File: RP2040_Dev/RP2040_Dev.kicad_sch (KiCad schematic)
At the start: 40 parts, among them J1 USB4105-GF-A, J2 Conn_01x18_Pin, J3 Conn_01x18_Pin, SW1 SW_Push, SW2 SW_Push, U1 RP2040, U2 W25Q128JVS, U4 AMS1117CS-3.3, Y1 ABM8G-12.000MHZ-4Y-T3

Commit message: rp2040 update
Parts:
- C1, C10, C11, C12, C13, C14, C15, C16, C17, C2, C3, C4, C5, C6, C7, C8, C9: footprint Capacitor_SMD:C_0402_1005Metric_Pad0.74x0.62mm_HandSolder -> Capacitor_SMD:C_0201_0603Metric_Pad0.64x0.40mm_HandSolder
- R1, R10, R2, R3, R4, R5, R6, R7, R8, R9: footprint Resistor_SMD:R_0402_1005Metric_Pad0.72x0.64mm_HandSolder -> Resistor_SMD:R_0201_0603Metric_Pad0.64x0.40mm_HandSolder
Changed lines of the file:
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@@
 			)
 		)
-		(property "Footprint" "Capacitor_SMD:C_0402_1005Metric_Pad0.74x0.62mm_HandSolder"
+		(property "Footprint" "Capacitor_SMD:C_0201_0603Metric_Pad0.64x0.40mm_HandSolder"
 			(at 146.05 63.5 0)
 			(effects
@@
 			)
 		)
-		(property "Footprint" "Capacitor_SMD:C_0402_1005Metric_Pad0.74x0.62mm_HandSolder"
+		(property "Footprint" "Capacitor_SMD:C_0201_0603Metric_Pad0.64x0.40mm_HandSolder"
 			(at 59.3852 121.92 0)
 			(effects
@@
 			)
 		)
-		(property "Footprint" "Capacitor_SMD:C_0402_1005Metric_Pad0.74x0.62mm_HandSolder"
+		(property "Footprint" "Capacitor_SMD:C_0201_0603Metric_Pad0.64x0.40mm_HandSolder"
 			(at 115.2652 160.02 0)
 			(effects
@@
 			)
 		)
-		(property "Footprint" "Capacitor_SMD:C_0402_1005Metric_Pad0.74x0.62mm_HandSolder"
+		(property "Footprint" "Capacitor_SMD:C_0201_0603Metric_Pad0.64x0.40mm_HandSolder"
 			(at 115.2652 40.64 0)
 			(effects
@@
 			)
 		)
-		(property "Footprint" "Capacitor_SMD:C_0402_1005Metric_Pad0.74x0.62mm_HandSolder"
+		(property "Footprint" "Capacitor_SMD:C_0201_0603Metric_Pad0.64x0.40mm_HandSolder"
 			(at 270.51 33.02 0)
 			(effects
@@
 			)
 		)
-		(property "Footprint" "Resistor_SMD:R_0402_1005Metric_Pad0.72x0.64mm_HandSolder"
+		(property "Footprint" "Resistor_SMD:R_0201_0603Metric_Pad0.64x0.40mm_HandSolder"
 			(at 160.528 167.64 90)
 			(effects
@@
 			)
 		)
-		(property "Footprint" "Capacitor_SMD:C_0402_1005Metric_Pad0.74x0.62mm_HandSolder"
+		(property "Footprint" "Capacitor_SMD:C_0201_0603Metric_Pad0.64x0.40mm_HandSolder"
 			(at 101.6 63.5 0)
 			(effects
@@
 			)
 		)
-		(property "Footprint" "Resistor_SMD:R_0402_1005Metric_Pad0.72x0.64mm_HandSolder"
+		(property "Footprint" "Resistor_SMD:R_0201_0603Metric_Pad0.64x0.40mm_HandSolder"
 			(at 208.28 40.64 0)
 			(effects
@@
 			)
 		)
-		(property "Footprint" "Resistor_SMD:R_0402_1005Metric_Pad0.72x0.64mm_HandSolder"
+		(property "Footprint" "Resistor_SMD:R_0201_0603Metric_Pad0.64x0.40mm_HandSolder"
 			(at 88.9 33.02 0)
 			(effects
@@
 			)
 		)
-		(property "Footprint" "Capacitor_SMD:C_0402_1005Metric_Pad0.74x0.62mm_HandSolder"
+		(property "Footprint" "Capacitor_SMD:C_0201_0603Metric_Pad0.64x0.40mm_HandSolder"
 			(at 154.94 63.5 0)
 			(effects
@@
 			)
 		)
-		(property "Footprint" "Resistor_SMD:R_0402_1005Metric_Pad0.72x0.64mm_HandSolder"
+		(property "Footprint" "Resistor_SMD:R_0201_0603Metric_Pad0.64x0.40mm_HandSolder"
 			(at 149.098 167.64 90)
 			(effects
@@
 			)
 		)
-		(property "Footprint" "Capacitor_SMD:C_0402_1005Metric_Pad0.74x0.62mm_HandSolder"
+		(property "Footprint" "Capacitor_SMD:C_0201_0603Metric_Pad0.64x0.40mm_HandSolder"
 			(at 110.49 63.5 0)
 			(effects
@@
 			)
 		)
-		(property "Footprint" "Resistor_SMD:R_0402_1005Metric_Pad0.72x0.64mm_HandSolder"
+		(property "Footprint" "Resistor_SMD:R_0201_0603Metric_Pad0.64x0.40mm_HandSolder"
 			(at 80.518 154.94 90)
 			(effects
@@
 			)
 		)
-		(property "Footprint" "Resistor_SMD:R_0402_1005Metric_Pad0.72x0.64mm_HandSolder"
+		(property "Footprint" "Resistor_SMD:R_0201_0603Metric_Pad0.64x0.40mm_HandSolder"
 			(at 88.392 102.87 90)
 			(effects
@@
 			)
 		)
-		(property "Footprint" "Resistor_SMD:R_0402_1005Metric_Pad0.72x0.64mm_HandSolder"
+		(property "Footprint" "Resistor_SMD:R_0201_0603Metric_Pad0.64x0.40mm_HandSolder"
 			(at 38.1 33.02 0)
 			(effects
@@
 			)
 		)
-		(property "Footprint" "Capacitor_SMD:C_0402_1005Metric_Pad0.74x0.62mm_HandSolder"
+		(property "Footprint" "Capacitor_SMD:C_0201_0603Metric_Pad0.64x0.40mm_HandSolder"
 			(at 232.41 30.48 0)
 			(effects
@@
 			)
 		)
-		(property "Footprint" "Capacitor_SMD:C_0402_1005Metric_Pad0.74x0.62mm_HandSolder"
+		(property "Footprint" "Capacitor_SMD:C_0201_0603Metric_Pad0.64x0.40mm_HandSolder"
 			(at 224.79 30.48 0)
 			(effects
@@
 			)
 		)
-		(property "Footprint" "Capacitor_SMD:C_0402_1005Metric_Pad0.74x0.62mm_HandSolder"
+		(property "Footprint" "Capacitor_SMD:C_0201_0603Metric_Pad0.64x0.40mm_HandSolder"
 			(at 217.17 30.48 0)
 			(effects
@@
 			)
 		)
-		(property "Footprint" "Capacitor_SMD:C_0402_1005Metric_Pad0.74x0.62mm_HandSolder"
+		(property "Footprint" "Capacitor_SMD:C_0201_0603Metric_Pad0.64x0.40mm_HandSolder"
 			(at 195.2752 124.46 0)
 			(effects
@@
 			)
 		)
-		(property "Footprint" "Resistor_SMD:R_0402_1005Metric_Pad0.72x0.64mm_HandSolder"
+		(property "Footprint" "Resistor_SMD:R_0201_0603Metric_Pad0.64x0.40mm_HandSolder"
 			(at 209.55 53.34 0)
 			(effects
@@
 			)
 		)
-		(property "Footprint" "Capacitor_SMD:C_0402_1005Metric_Pad0.74x0.62mm_HandSolder"
+		(property "Footprint" "Capacitor_SMD:C_0201_0603Metric_Pad0.64x0.40mm_HandSolder"
 			(at 128.27 63.5 0)
 			(effects
@@
 			)
 		)
-		(property "Footprint" "Capacitor_SMD:C_0402_1005Metric_Pad0.74x0.62mm_HandSolder"
+		(property "Footprint" "Capacitor_SMD:C_0201_0603Metric_Pad0.64x0.40mm_HandSolder"
 			(at 137.16 63.5 0)
 			(effects
@@
 			)
 		)
-		(property "Footprint" "Capacitor_SMD:C_0402_1005Metric_Pad0.74x0.62mm_HandSolder"
+		(property "Footprint" "Capacitor_SMD:C_0201_0603Metric_Pad0.64x0.40mm_HandSolder"
 			(at 119.38 63.5 0)
 			(effects
@@
 			)
 		)
-		(property "Footprint" "Resistor_SMD:R_0402_1005Metric_Pad0.72x0.64mm_HandSolder"
+		(property "Footprint" "Resistor_SMD:R_0201_0603Metric_Pad0.64x0.40mm_HandSolder"
 			(at 68.58 164.338 90)
 			(effects
@@
 			)
 		)
-		(property "Footprint" "Capacitor_SMD:C_0402_1005Metric_Pad0.74x0.62mm_HandSolder"
+		(property "Footprint" "Capacitor_SMD:C_0201_0603Metric_Pad0.64x0.40mm_HandSolder"
 			(at 143.2052 40.64 0)
 			(effects
@@
 			)
 		)
-		(property "Footprint" "Resistor_SMD:R_0402_1005Metric_Pad0.72x0.64mm_HandSolder"
+		(property "Footprint" "Resistor_SMD:R_0201_0603Metric_Pad0.64x0.40mm_HandSolder"
 			(at 209.55 55.88 0)
 			(effects
@@
 			)
 		)
-		(property "Footprint" "Capacitor_SMD:C_0402_1005Metric_Pad0.74x0.62mm_HandSolder"
+		(property "Footprint" "Capacitor_SMD:C_0201_0603Metric_Pad0.64x0.40mm_HandSolder"
 			(at 91.1352 121.92 0)
 			(effects

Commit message: Cleaned up atmega and made atmega32 README
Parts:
- removed C11: 0.1u, Capacitor_SMD:C_0201_0603Metric_Pad0.64x0.40mm_HandSolder, symbol Device:C_Small
- renumbered C17 to C11
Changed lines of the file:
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@@
 	(wire
 		(pts
-			(xy 154.94 69.85) (xy 154.94 66.04)
-		)
-		(stroke
-			(width 0)
-			(type default)
-		)
-	)
-	(wire
-		(pts
 			(xy 83.82 175.26) (xy 88.9 175.26)
 		)
@@
 	(wire
 		(pts
-			(xy 146.05 69.85) (xy 154.94 69.85)
-		)
-		(stroke
-			(width 0)
-			(type default)
-		)
-	)
-	(wire
-		(pts
 			(xy 128.27 55.88) (xy 137.16 55.88)
 		)
@@
 	(wire
 		(pts
-			(xy 154.94 55.88) (xy 154.94 60.96)
-		)
-		(stroke
-			(width 0)
-			(type default)
-		)
-	)
-	(wire
-		(pts
 			(xy 194.31 124.46) (xy 194.31 128.27)
 		)
@@
 	(wire
 		(pts
-			(xy 146.05 55.88) (xy 154.94 55.88)
-		)
-		(stroke
-			(width 0)
-			(type default)
-		)
-	)
-	(wire
-		(pts
 			(xy 234.95 35.56) (xy 234.95 38.1)
 		)
@@
 	)
 	(symbol
-		(lib_id "Device:C_Small")
-		(at 154.94 63.5 0)
-		(mirror y)
-		(unit 1)
-		(exclude_from_sim no)
-		(in_bom yes)
-		(on_board yes)
-		(dnp no)
-		(property "Reference" "C11"
-			(at 161.036 62.23 0)
-			(effects
-				(font
-					(size 1.27 1.27)
-				)
-				(justify left)
-			)
-		)
-		(property "Value" "0.1u"
-			(at 161.036 64.77 0)
-			(effects
-				(font
-					(size 1.27 1.27)
-				)
-				(justify left)
-			)
-		)
-		(property "Footprint" "Capacitor_SMD:C_0201_0603Metric_Pad0.64x0.40mm_HandSolder"
-			(at 154.94 63.5 0)
-			(effects
-				(font
-					(size 1.27 1.27)
-				)
-				(hide yes)
-			)
-		)
-		(property "Datasheet" "~"
-			(at 154.94 63.5 0)
-			(effects
-				(font
-					(size 1.27 1.27)
-				)
-				(hide yes)
-			)
-		)
-		(property "Description" "Unpolarized capacitor, small symbol"
-			(at 154.94 63.5 0)
-			(effects
-				(font
-					(size 1.27 1.27)
-				)
-				(hide yes)
-			)
-		)
-		(pin "2"
-		)
-		(pin "1"
-		)
-		(instances
-			(project "RP2040_Dev"
-				(path "/59019ba2-5ef7-4631-99cf-04fb9aa8a151"
-					(reference "C11")
-					(unit 1)
-				)
-			)
-		)
-	)
-	(symbol
 		(lib_id "Device:R")
 		(at 147.32 167.64 180)
@@
 		(on_board yes)
 		(dnp no)
-		(property "Reference" "C17"
+		(property "Reference" "C11"
 			(at 198.12 119.3799 0)
 			(effects
@@
 			(project "RP2040_Dev"
 				(path "/59019ba2-5ef7-4631-99cf-04fb9aa8a151"
-					(reference "C17")
+					(reference "C11")
 					(unit 1)
 				)

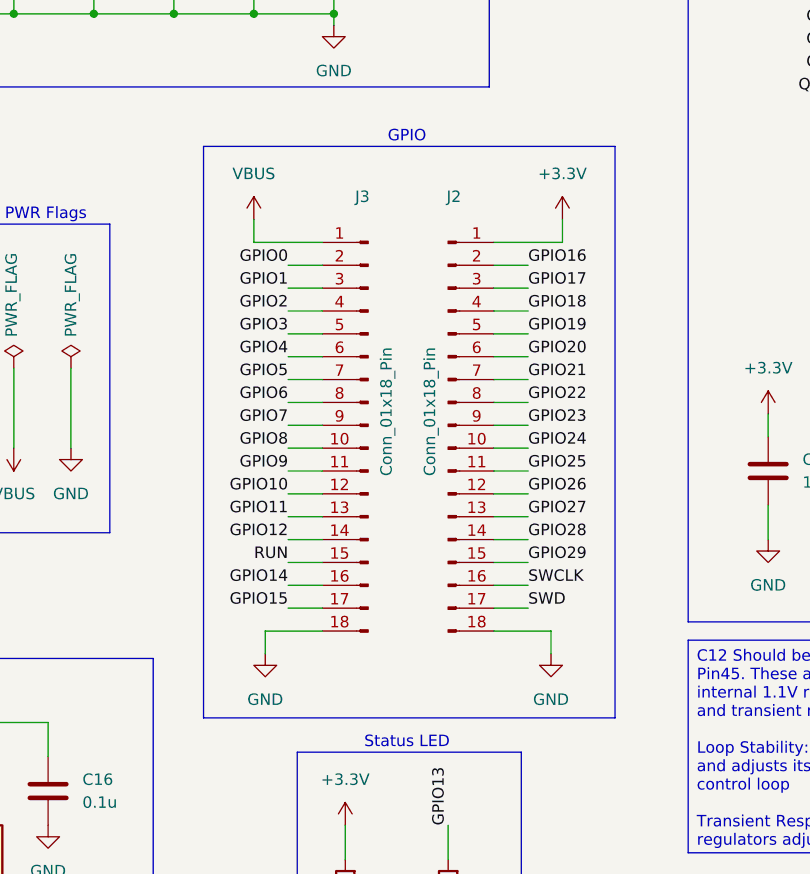
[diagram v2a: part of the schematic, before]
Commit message: Added additional board folders, updataed RP2040, ATmega, and ESP32
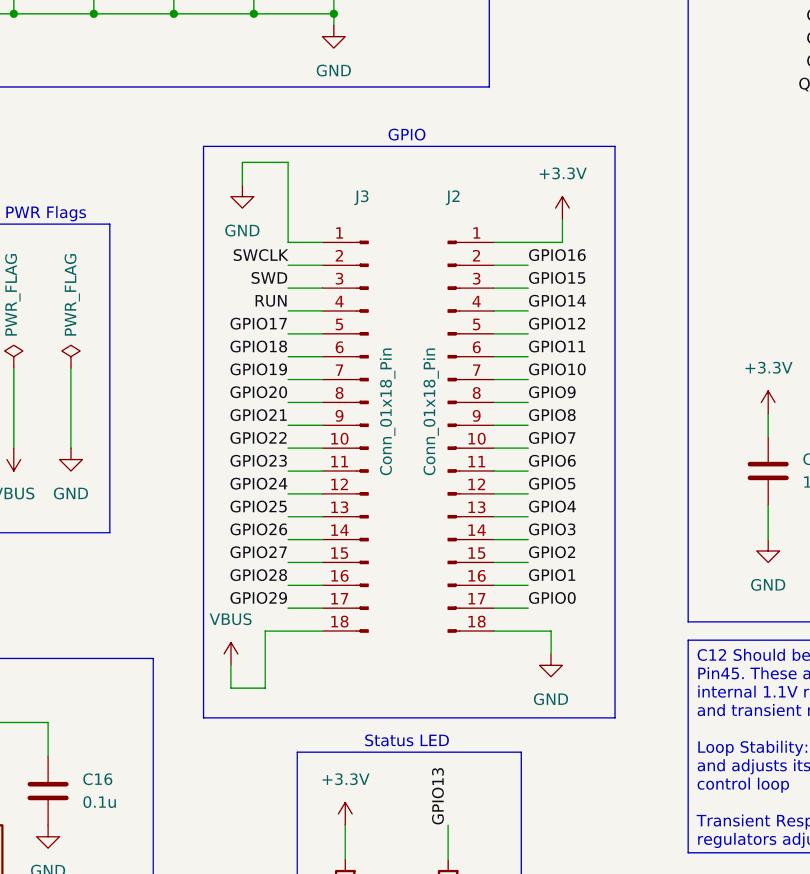
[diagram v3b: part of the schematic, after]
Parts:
- C1, C10, C11, C12, C13, C14, C15, C16, C2, C3, C4, C5, C6, C7, C8, C9: footprint Capacitor_SMD:C_0201_0603Metric_Pad0.64x0.40mm_HandSolder -> Capacitor_SMD:C_0402_1005Metric
- R10, R7, R8, R9: footprint Resistor_SMD:R_0201_0603Metric_Pad0.64x0.40mm_HandSolder -> Resistor_SMD:R_0402_1005Metric
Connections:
- net GND: now also J3.1 (Pin_1); no longer J3.18 (Pin_18)
- net GPIO0: now also J2.17 (Pin_17); no longer J3.2 (Pin_2)
- net GPIO1: now also J2.16 (Pin_16); no longer J3.3 (Pin_3)
- net GPIO10: now also J2.7 (Pin_7); no longer J3.12 (Pin_12)
- net GPIO11: now also J2.6 (Pin_6); no longer J3.13 (Pin_13)
- net GPIO12: now also J2.5 (Pin_5); no longer J3.14 (Pin_14)
- net GPIO14: now also J2.4 (Pin_4); no longer J3.16 (Pin_16)
- net GPIO15: now also J2.3 (Pin_3); no longer J3.17 (Pin_17)
- net GPIO17: now also J3.5 (Pin_5); no longer J2.3 (Pin_3)
- net GPIO18: now also J3.6 (Pin_6); no longer J2.4 (Pin_4)
- net GPIO19: now also J3.7 (Pin_7); no longer J2.5 (Pin_5)
- net GPIO2: now also J2.15 (Pin_15); no longer J3.4 (Pin_4)
- net GPIO20: now also J3.8 (Pin_8); no longer J2.6 (Pin_6)
- net GPIO21: now also J3.9 (Pin_9); no longer J2.7 (Pin_7)
- net GPIO22: now also J3.10 (Pin_10); no longer J2.8 (Pin_8)
- net GPIO23: now also J3.11 (Pin_11); no longer J2.9 (Pin_9)
- net GPIO24: now also J3.12 (Pin_12); no longer J2.10 (Pin_10)
- net GPIO25: now also J3.13 (Pin_13); no longer J2.11 (Pin_11)
- net GPIO26: now also J3.14 (Pin_14); no longer J2.12 (Pin_12)
- net GPIO27: now also J3.15 (Pin_15); no longer J2.13 (Pin_13)
- net GPIO28: now also J3.16 (Pin_16); no longer J2.14 (Pin_14)
- net GPIO29: now also J3.17 (Pin_17); no longer J2.15 (Pin_15)
- net GPIO3: now also J2.14 (Pin_14); no longer J3.5 (Pin_5)
- net GPIO4: now also J2.13 (Pin_13); no longer J3.6 (Pin_6)
- net GPIO5: now also J2.12 (Pin_12); no longer J3.7 (Pin_7)
- net GPIO6: now also J2.11 (Pin_11); no longer J3.8 (Pin_8)
- net GPIO7: now also J2.10 (Pin_10); no longer J3.9 (Pin_9)
- net GPIO8: now also J2.9 (Pin_9); no longer J3.10 (Pin_10)
- net GPIO9: now also J2.8 (Pin_8); no longer J3.11 (Pin_11)
- net RUN: now also J3.4 (Pin_4); no longer J3.15 (Pin_15)
- net SWCLK: now also J3.2 (Pin_2); no longer J2.16 (Pin_16)
- net SWD: now also J3.3 (Pin_3); no longer J2.17 (Pin_17)
- net VBUS: now also J3.18 (Pin_18); no longer J3.1 (Pin_1)
